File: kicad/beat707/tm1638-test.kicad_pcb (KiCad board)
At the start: 2 copper layers, 100 x 100 mm, 80 parts, among them J1 Conn_01x05_Male, SW1 SW_Push, SW10 SW_Push, SW11 SW_Push, SW12 SW_Push, SW13 SW_Push, SW14 SW_Push, SW15 SW_Push, SW16 SW_Push, SW17 SW_Push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

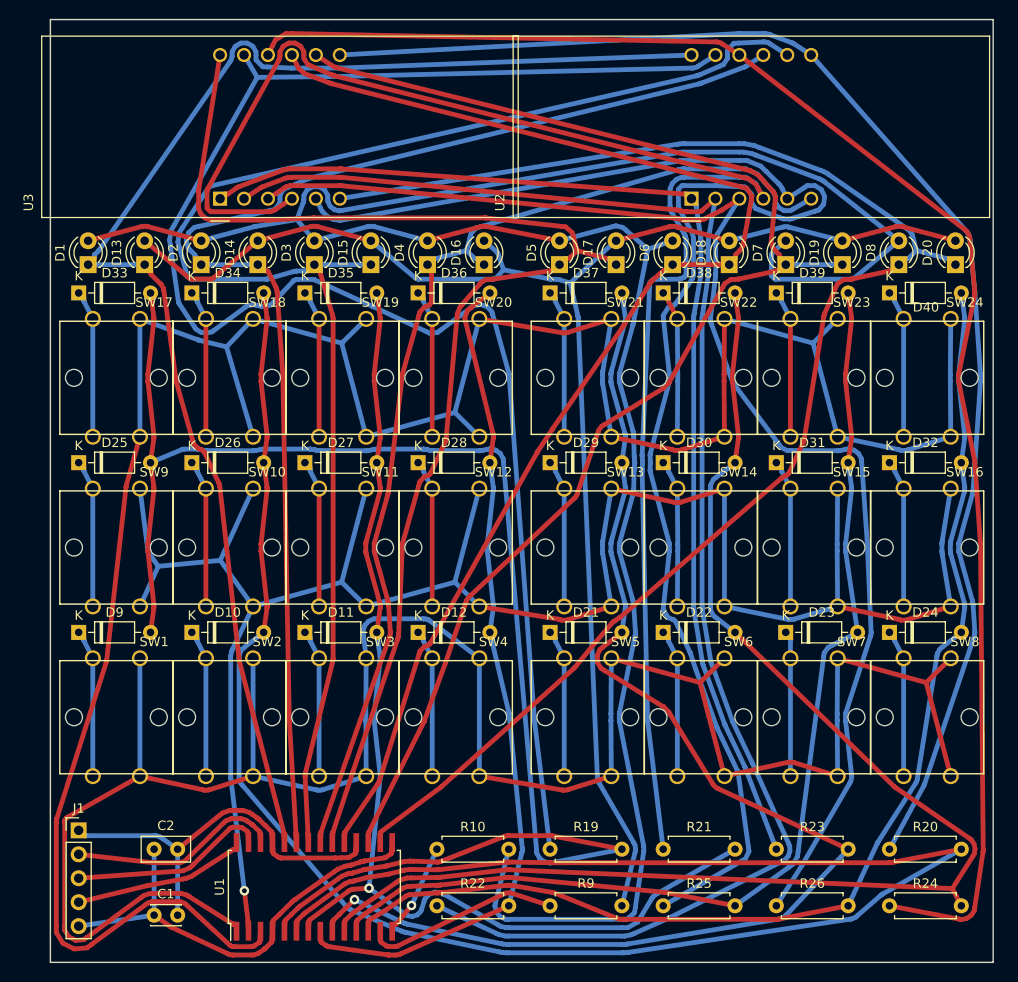
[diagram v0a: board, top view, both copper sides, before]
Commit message: removed unneded files
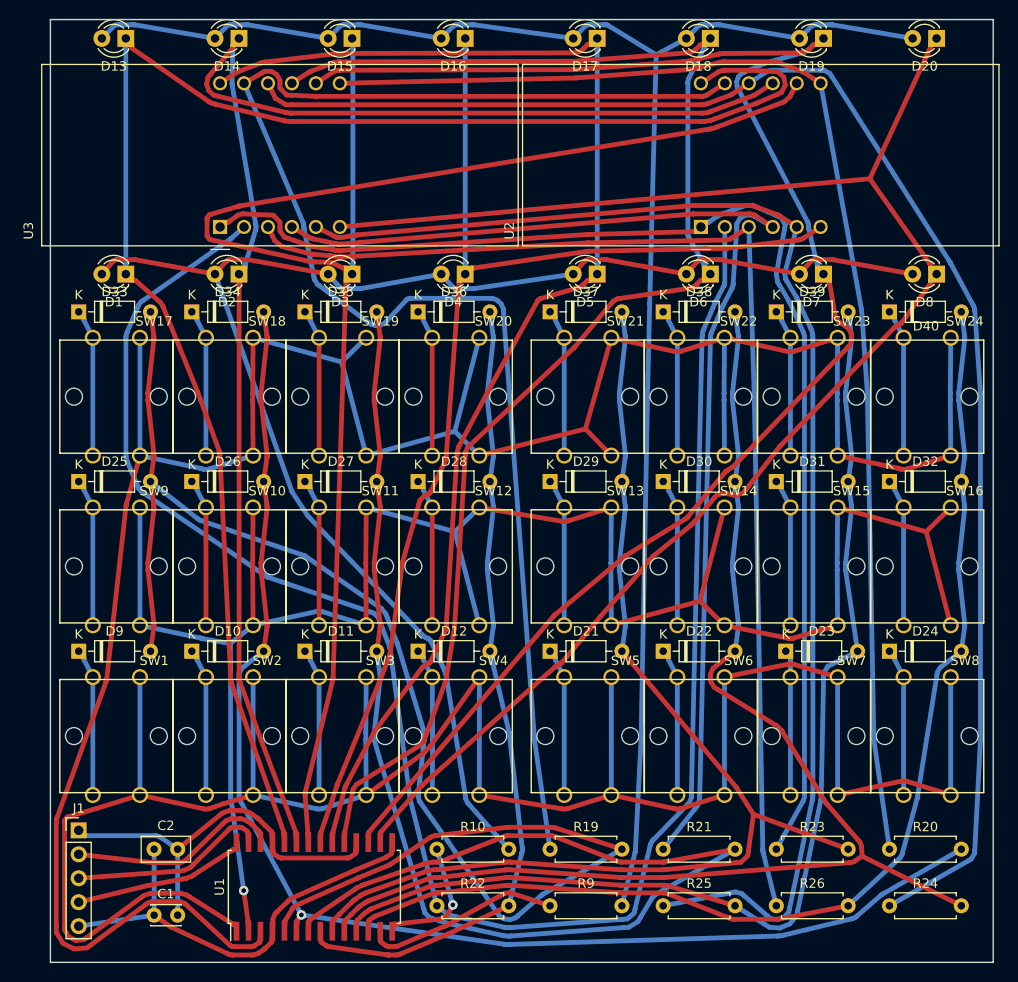
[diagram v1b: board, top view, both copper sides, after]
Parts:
- moved D13 24.1 mm to (138.0, 82.0), turned to 180 degrees
- moved D14 24.1 mm to (150.0, 82.0), turned to 180 degrees
- moved D15 24.1 mm to (162.0, 82.0), turned to 180 degrees
- moved D16 24.1 mm to (174.0, 82.0), turned to 180 degrees
- moved D17 24.1 mm to (188.0, 82.0), turned to 180 degrees
- moved D18 24.1 mm to (200.0, 82.0), turned to 180 degrees
- moved D19 24.1 mm to (212.0, 82.0), turned to 180 degrees
- moved D20 24.1 mm to (224.0, 82.0), turned to 180 degrees
- moved D1 4.12 mm to (138.0, 107.0), turned to 180 degrees
- moved D2 4.12 mm to (150.0, 107.0), turned to 180 degrees
- moved D3 4.12 mm to (162.0, 107.0), turned to 180 degrees
- moved D4 4.12 mm to (174.0, 107.0), turned to 180 degrees
- moved D5 4.12 mm to (188.0, 107.0), turned to 180 degrees
- moved D6 4.12 mm to (200.0, 107.0), turned to 180 degrees
- moved D7 4.12 mm to (212.0, 107.0), turned to 180 degrees
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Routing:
- net Net-(D1-Pad2): track 250.2 -> 162.1 mm
- net /TM1638 Module/SEG2: track 212.5 -> 141.6 mm, vias 0 -> 1
- net Net-(R21-Pad1): track 169.6 -> 124.7 mm
- net /TM1638 Module/SEG3: track 117.6 -> 150.3 mm, vias 1 -> 0
- net Net-(R22-Pad1): track 162.9 -> 191.3 mm
- net /TM1638 Module/GRID7: track 144.9 -> 171.0 mm
- net /TM1638 Module/GRID1: track 148.3 -> 173.3 mm
- net Net-(R25-Pad1): track 162.5 -> 140.5 mm
- net Net-(R19-Pad1): track 175.0 -> 156.5 mm
- net /TM1638 Module/GRID2: track 137.3 -> 155.1 mm
- net Net-(D13-Pad2): track 165.6 -> 182.6 mm
- net /TM1638 Module/SEG5: track 136.4 -> 120.7 mm, vias 1 -> 0
- net Net-(R26-Pad1): track 139.6 -> 124.9 mm
- net /TM1638 Module/GRID6: track 137.3 -> 151.4 mm
- net /TM1638 Module/GRID4: track 112.8 -> 126.8 mm
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
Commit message: new FRAM test and TM!638 board cleanups
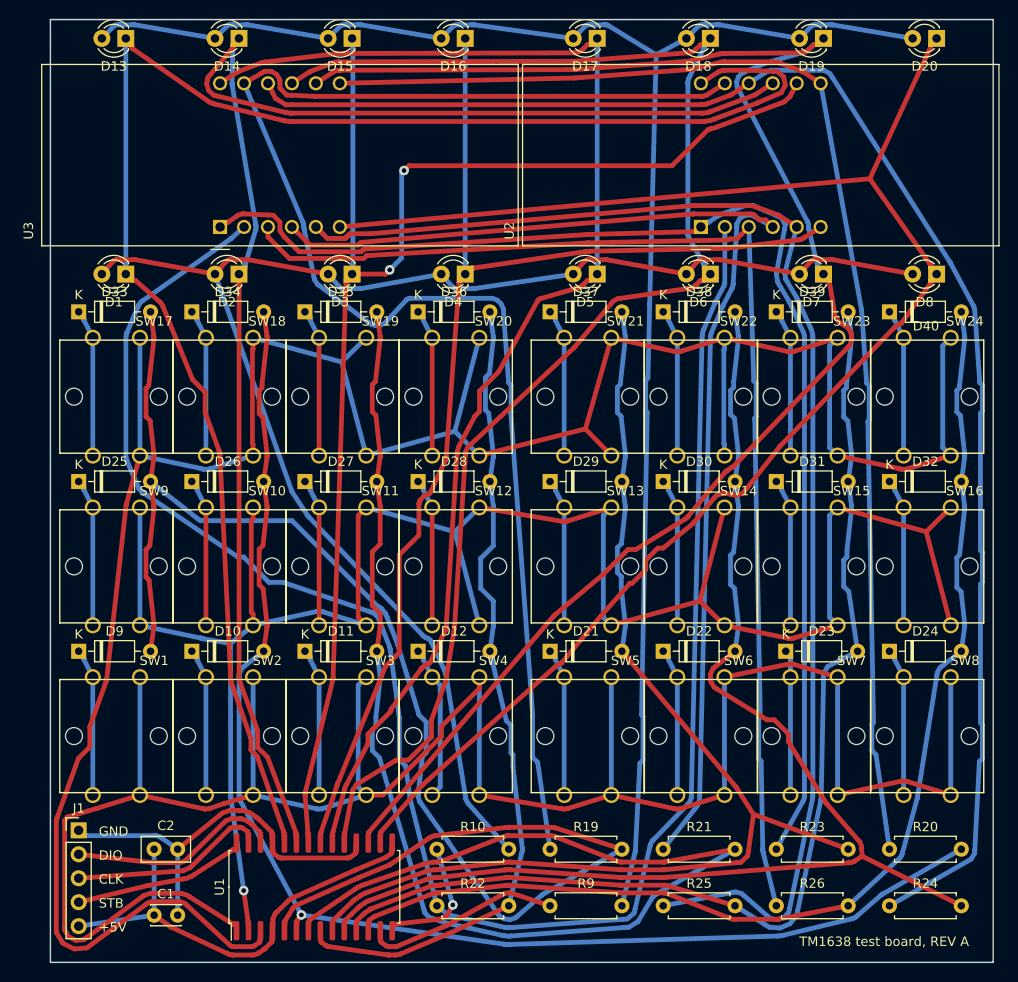
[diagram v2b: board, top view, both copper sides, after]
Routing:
- net /TM1638 Module/GRID3: track 169.2 -> 146.4 mm, vias 0 -> 2
- net /TM1638 Module/SEG1: track 155.9 -> 158.3 mm
- net /TM1638 Module/K2: track 216.1 -> 218.4 mm
- net Net-(R25-Pad1): track 140.5 -> 142.6 mm
- net /TM1638 Module/K3: track 263.9 -> 265.7 mm
- net /TM1638 Module/SEG4: track 86.1 -> 87.9 mm
- net /TM1638 Module/K1: track 235.8 -> 237.5 mm
- net /TM1638 Module/SEG3: track 150.3 -> 151.6 mm
- net Net-(R26-Pad1): track 124.9 -> 126.2 mm
- net /TM1638 Module/GRID4: track 126.8 -> 127.9 mm
- net /TM1638 Module/SEG6: track 135.2 -> 136.2 mm
- net Net-(D12-Pad1): track 15.7 -> 16.4 mm
- net /TM1638 Module/GRID5: track 136.4 -> 137.1 mm
- net Net-(R21-Pad1): track 124.7 -> 125.3 mm
- net /TM1638 Module/SEG7: track 116.9 -> 117.5 mm
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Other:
- net class Default: clearance 0.254 -> 0.2032
- rule trace_clearance: 0.254 -> 0.2032
- board text added: "+5V"
- board text added: "CLK"
- board text added: "DIO"
- board text added: "GND"
- board text added: "STB"
- board text added: "TM1638 test board, REV A"
